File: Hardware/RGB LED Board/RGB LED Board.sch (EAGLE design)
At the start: 9 parts, among them U1 WS2801

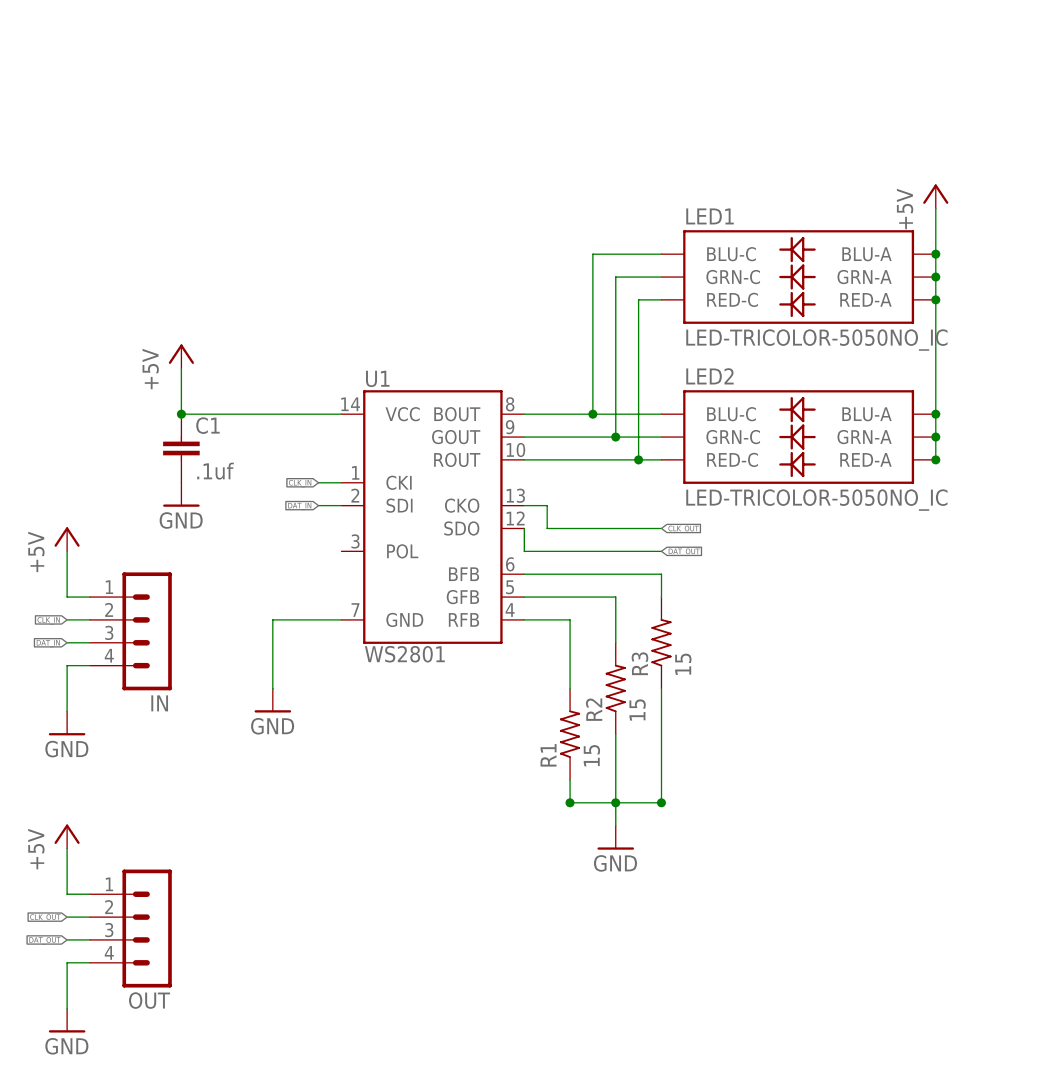
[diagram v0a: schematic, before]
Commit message: changed LED to CLY6D-FKC-CK1N1D1BB7D3D3
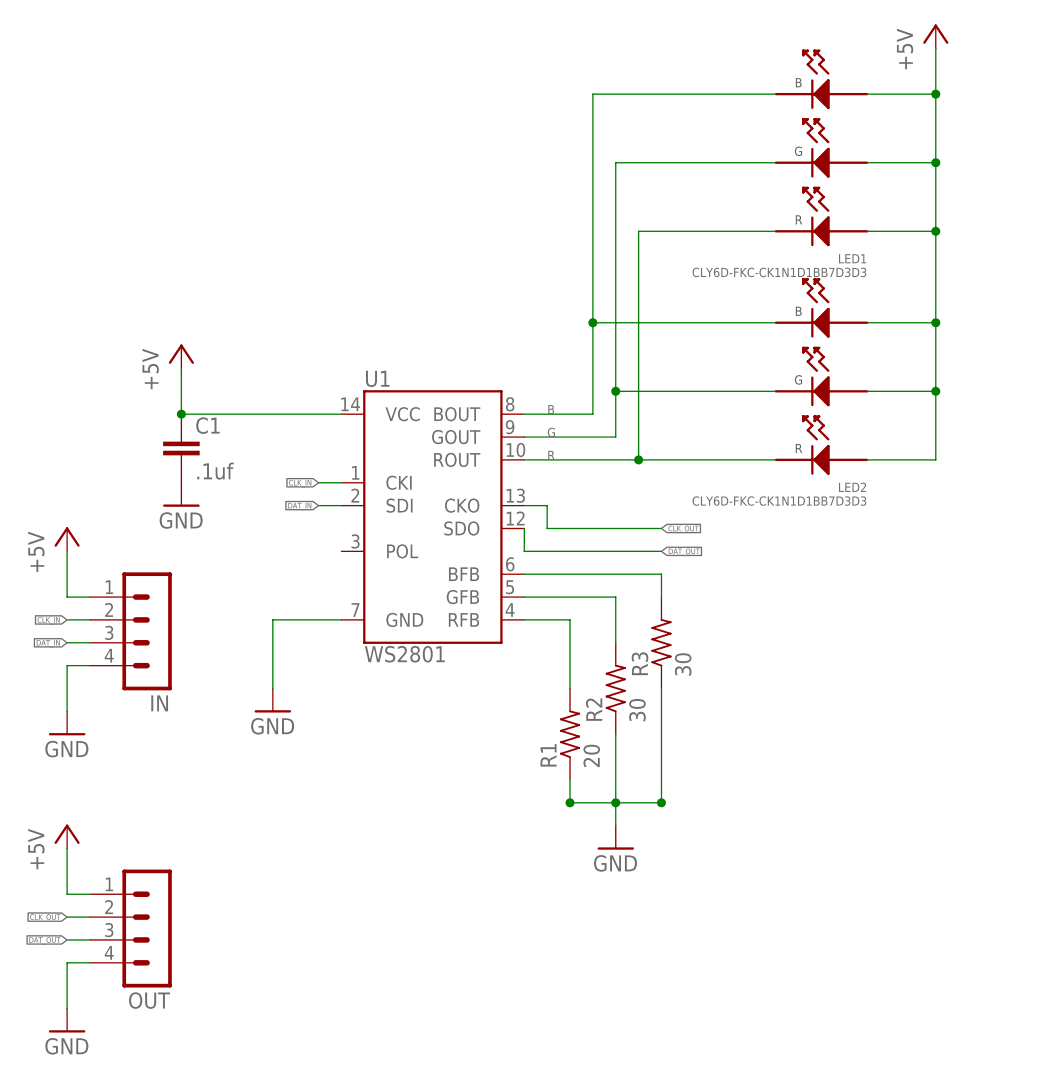
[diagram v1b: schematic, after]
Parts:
- LED1, LED2: value LED-TRICOLOR-5050NO_IC -> CLY6D-FKC-CK1N1D1BB7D3D3; device SparkFun-LED:LED-TRICOLOR-5050NO_IC -> PP_LED:CLY6D-FKC
- R1: value 15 -> 20
- R2, R3: value 15 -> 30
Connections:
- net 456456456 renamed RFB
- net BG renamed BFB
- net GG renamed GFB
- net +5V: now also LED1.ANODE_BLUE, LED1.ANODE_GREEN, LED1.ANODE_RED, LED2.ANODE_BLUE, LED2.ANODE_GREEN, LED2.ANODE_RED; no longer LED1.BLU-A, LED1.GRN-A, LED1.RED-A, LED2.BLU-A, LED2.GRN-A, LED2.RED-A
- net B: now also LED1.CATHODE_BLUE, LED2.CATHODE_BLUE; no longer LED1.BLU-C, LED2.BLU-C
- net G: now also LED1.CATHODE_GREEN, LED2.CATHODE_GREEN; no longer LED1.GRN-C, LED2.GRN-C
- net R: now also LED1.CATHODE_RED, LED2.CATHODE_RED; no longer LED1.RED-C, LED2.RED-C
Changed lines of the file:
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@@
 <part name="GND2" library="supply1" deviceset="GND" device=""/>
 <part name="C1" library="SparkFun-Capacitors" deviceset="CAP" device="0805" value=".1uf"/>
-<part name="R1" library="resistor" deviceset="R-US_" device="R0805" value="15"/>
-<part name="R2" library="resistor" deviceset="R-US_" device="R0805" value="15"/>
-<part name="R3" library="resistor" deviceset="R-US_" device="R0805" value="15"/>
+<part name="R1" library="resistor" deviceset="R-US_" device="R0805" value="20"/>
+<part name="R2" library="resistor" deviceset="R-US_" device="R0805" value="30"/>
+<part name="R3" library="resistor" deviceset="R-US_" device="R0805" value="30"/>
 <part name="GND3" library="supply1" deviceset="GND" device=""/>
-<part name="LED1" library="SparkFun-LED" deviceset="LED-TRICOLOR-5050" device="NO_IC"/>
 <part name="P+2" library="supply1" deviceset="+5V" device=""/>
 <part name="GND4" library="supply1" deviceset="GND" device=""/>
@@
 <part name="P+4" library="supply1" deviceset="+5V" device=""/>
 <part name="GND5" library="supply1" deviceset="GND" device=""/>
-<part name="LED2" library="SparkFun-LED" deviceset="LED-TRICOLOR-5050" device="NO_IC"/>
 <part name="IN" library="con-lstb" deviceset="MA04-1" device=""/>
 <part name="OUT" library="con-lstb" deviceset="MA04-1" device=""/>
+<part name="LED1" library="PP_LED" deviceset="CLY6D-FKC" device="" value="CLY6D-FKC-CK1N1D1BB7D3D3"/>
+<part name="LED2" library="PP_LED" deviceset="CLY6D-FKC" device="" value="CLY6D-FKC-CK1N1D1BB7D3D3"/>
 </parts>
 <sheets>
@@
 <instance part="R3" gate="G$1" x="93.98" y="27.94" rot="R90"/>
 <instance part="GND3" gate="1" x="88.9" y="5.08"/>
-<instance part="LED1" gate="D1" x="109.22" y="68.58"/>
-<instance part="P+2" gate="1" x="124.46" y="78.74"/>
+<instance part="P+2" gate="1" x="124.46" y="96.52"/>
 <instance part="GND4" gate="1" x="27.94" y="17.78"/>
 <instance part="P+3" gate="1" x="27.94" y="40.64"/>
 <instance part="P+4" gate="1" x="27.94" y="7.62"/>
 <instance part="GND5" gate="1" x="27.94" y="-15.24"/>
-<instance part="LED2" gate="D1" x="109.22" y="50.8"/>
 <instance part="IN" gate="1" x="38.1" y="27.94" rot="R180"/>
 <instance part="OUT" gate="1" x="38.1" y="-5.08" rot="R180"/>
+<instance part="LED1" gate="G$1" x="111.76" y="81.28" rot="MR0"/>
+<instance part="LED2" gate="G$1" x="111.76" y="55.88" rot="MR0"/>
 </instances>
 <busses>
@@
 </segment>
 <segment>
-<pinref part="LED1" gate="D1" pin="RED-A"/>
-<pinref part="LED1" gate="D1" pin="GRN-A"/>
-<wire x1="124.46" y1="66.04" x2="124.46" y2="68.58" width="0.1524" layer="91"/>
-<pinref part="LED1" gate="D1" pin="BLU-A"/>
-<wire x1="124.46" y1="68.58" x2="124.46" y2="71.12" width="0.1524" layer="91"/>
-<pinref part="P+2" gate="1" pin="+5V"/>
-<wire x1="124.46" y1="71.12" x2="124.46" y2="76.2" width="0.1524" layer="91"/>
-<junction x="124.46" y="71.12"/>
-<junction x="124.46" y="68.58"/>
-<junction x="124.46" y="66.04"/>
-<pinref part="LED2" gate="D1" pin="RED-A"/>
-<pinref part="LED2" gate="D1" pin="GRN-A"/>
-<wire x1="124.46" y1="48.26" x2="124.46" y2="50.8" width="0.1524" layer="91"/>
-<pinref part="LED2" gate="D1" pin="BLU-A"/>
-<wire x1="124.46" y1="50.8" x2="124.46" y2="53.34" width="0.1524" layer="91"/>
-<wire x1="124.46" y1="53.34" x2="124.46" y2="66.04" width="0.1524" layer="91"/>
-<junction x="124.46" y="48.26"/>
-<junction x="124.46" y="50.8"/>
-<junction x="124.46" y="53.34"/>
-</segment>
-<segment>
 <wire x1="30.48" y1="33.02" x2="27.94" y2="33.02" width="0.1524" layer="91"/>
 <wire x1="27.94" y1="33.02" x2="27.94" y2="38.1" width="0.1524" layer="91"/>
@@
 <pinref part="OUT" gate="1" pin="1"/>
 </segment>
-</net>
-<net name="456456456" class="0">
+<segment>
+<pinref part="LED2" gate="G$1" pin="ANODE_RED"/>
+<pinref part="P+2" gate="1" pin="+5V"/>
+<wire x1="116.84" y1="48.26" x2="124.46" y2="48.26" width="0.1524" layer="91"/>
+<wire x1="124.46" y1="48.26" x2="124.46" y2="55.88" width="0.1524" layer="91"/>
+<pinref part="LED1" gate="G$1" pin="ANODE_BLUE"/>
+<wire x1="124.46" y1="55.88" x2="124.46" y2="63.5" width="0.1524" layer="91"/>
+<wire x1="124.46" y1="63.5" x2="124.46" y2="73.66" width="0.1524" layer="91"/>
+<wire x1="124.46" y1="73.66" x2="124.46" y2="81.28" width="0.1524" layer="91"/>
+<wire x1="124.46" y1="81.28" x2="124.46" y2="88.9" width="0.1524" layer="91"/>
+<wire x1="124.46" y1="88.9" x2="124.46" y2="93.98" width="0.1524" layer="91"/>
+<wire x1="116.84" y1="88.9" x2="124.46" y2="88.9" width="0.1524" layer="91"/>
+<pinref part="LED1" gate="G$1" pin="ANODE_GREEN"/>
+<wire x1="116.84" y1="81.28" x2="124.46" y2="81.28" width="0.1524" layer="91"/>
+<pinref part="LED1" gate="G$1" pin="ANODE_RED"/>
+<wire x1="116.84" y1="73.66" x2="124.46" y2="73.66" width="0.1524" layer="91"/>
+<pinref part="LED2" gate="G$1" pin="ANODE_BLUE"/>
+<wire x1="116.84" y1="63.5" x2="124.46" y2="63.5" width="0.1524" layer="91"/>
+<pinref part="LED2" gate="G$1" pin="ANODE_GREEN"/>
+<wire x1="116.84" y1="55.88" x2="124.46" y2="55.88" width="0.1524" layer="91"/>
+<junction x="124.46" y="88.9"/>
+<junction x="124.46" y="81.28"/>
+<junction x="124.46" y="73.66"/>
+<junction x="124.46" y="63.5"/>
+<junction x="124.46" y="55.88"/>
+</segment>
+</net>
+<net name="RFB" class="0">
 <segment>
 <pinref part="U1" gate="G$1" pin="RFB"/>
@@
 </segment>
 </net>
-<net name="GG" class="0">
+<net name="GFB" class="0">
 <segment>
 <pinref part="U1" gate="G$1" pin="GFB"/>
@@
 </segment>
 </net>
-<net name="BG" class="0">
+<net name="BFB" class="0">
 <segment>
 <pinref part="U1" gate="G$1" pin="BFB"/>
@@
 <segment>
 <pinref part="U1" gate="G$1" pin="BOUT"/>
-<pinref part="LED2" gate="D1" pin="BLU-C"/>
 <wire x1="78.74" y1="53.34" x2="86.36" y2="53.34" width="0.1524" layer="91"/>
-<pinref part="LED1" gate="D1" pin="BLU-C"/>
-<wire x1="86.36" y1="53.34" x2="93.98" y2="53.34" width="0.1524" layer="91"/>
-<wire x1="93.98" y1="71.12" x2="86.36" y2="71.12" width="0.1524" layer="91"/>
-<wire x1="86.36" y1="71.12" x2="86.36" y2="53.34" width="0.1524" layer="91"/>
-<junction x="86.36" y="53.34"/>
+<label x="81.28" y="53.34" size="1.016" layer="95" font="vector"/>
+<pinref part="LED1" gate="G$1" pin="CATHODE_BLUE"/>
+<wire x1="106.68" y1="88.9" x2="86.36" y2="88.9" width="0.1524" layer="91"/>
+<wire x1="86.36" y1="88.9" x2="86.36" y2="63.5" width="0.1524" layer="91"/>
+<pinref part="LED2" gate="G$1" pin="CATHODE_BLUE"/>
+<wire x1="86.36" y1="63.5" x2="86.36" y2="53.34" width="0.1524" layer="91"/>
+<wire x1="106.68" y1="63.5" x2="86.36" y2="63.5" width="0.1524" layer="91"/>
+<junction x="86.36" y="63.5"/>
 </segment>
 </net>
 <net name="G" class="0">
 <segment>
-<pinref part="LED2" gate="D1" pin="GRN-C"/>
 <pinref part="U1" gate="G$1" pin="GOUT"/>
-<wire x1="93.98" y1="50.8" x2="88.9" y2="50.8" width="0.1524" layer="91"/>
-<pinref part="LED1" gate="D1" pin="GRN-C"/>
 <wire x1="88.9" y1="50.8" x2="78.74" y2="50.8" width="0.1524" layer="91"/>
-<wire x1="93.98" y1="68.58" x2="88.9" y2="68.58" width="0.1524" layer="91"/>
-<wire x1="88.9" y1="68.58" x2="88.9" y2="50.8" width="0.1524" layer="91"/>
-<junction x="88.9" y="50.8"/>
+<label x="81.28" y="50.8" size="1.016" layer="95" font="vector"/>
+<pinref part="LED2" gate="G$1" pin="CATHODE_GREEN"/>
+<wire x1="88.9" y1="55.88" x2="88.9" y2="50.8" width="0.1524" layer="91"/>
+<wire x1="106.68" y1="55.88" x2="88.9" y2="55.88" width="0.1524" layer="91"/>
+<pinref part="LED1" gate="G$1" pin="CATHODE_GREEN"/>
+<wire x1="106.68" y1="81.28" x2="88.9" y2="81.28" width="0.1524" layer="91"/>
+<wire x1="88.9" y1="81.28" x2="88.9" y2="55.88" width="0.1524" layer="91"/>
+<junction x="88.9" y="55.88"/>
 </segment>
 </net>
@@
 <segment>
 <pinref part="U1" gate="G$1" pin="ROUT"/>
-<pinref part="LED2" gate="D1" pin="RED-C"/>
 <wire x1="78.74" y1="48.26" x2="91.44" y2="48.26" width="0.1524" layer="91"/>
-<pinref part="LED1" gate="D1" pin="RED-C"/>
-<wire x1="91.44" y1="48.26" x2="93.98" y2="48.26" width="0.1524" layer="91"/>
-<wire x1="93.98" y1="66.04" x2="91.44" y2="66.04" width="0.1524" layer="91"/>
-<wire x1="91.44" y1="66.04" x2="91.44" y2="48.26" width="0.1524" layer="91"/>
+<wire x1="91.44" y1="73.66" x2="91.44" y2="48.26" width="0.1524" layer="91"/>
+<label x="81.28" y="48.26" size="1.016" layer="95" font="vector"/>
+<pinref part="LED2" gate="G$1" pin="CATHODE_RED"/>
+<wire x1="91.44" y1="48.26" x2="106.68" y2="48.26" width="0.1524" layer="91"/>
+<pinref part="LED1" gate="G$1" pin="CATHODE_RED"/>
+<wire x1="91.44" y1="73.66" x2="106.68" y2="73.66" width="0.1524" layer="91"/>
 <junction x="91.44" y="48.26"/>
 </segment>
